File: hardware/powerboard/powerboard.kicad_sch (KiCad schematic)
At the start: 31 parts, among them J1 USB_B_Micro, U1 AP2138N-2.5, U2 MCP1603, U3 RP2040

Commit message: Slight schematic changes
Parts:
- added C19, C20, C21: 1n, Capacitor_SMD:C_0603_1608Metric, symbol Device:C
- added C22: 10u, Capacitor_SMD:C_0603_1608Metric, symbol Device:C
- added R10, R11, R6, R7, R8, R9: 1k, Resistor_SMD:R_0603_1608Metric, symbol Device:R
- added SW1: Oct_Up, Button_Switch_THT:SW_PUSH_6mm, symbol Switch:SW_Push
- added SW2: RESET, Button_Switch_THT:SW_PUSH_6mm, symbol Switch:SW_Push
- added SW3: Oct_Down, Button_Switch_THT:SW_PUSH_6mm, symbol Switch:SW_Push
- C1, C10, C11, C12, C13, C14, C15, C2, C3, C4, C5, C6, C8: footprint (none) -> Capacitor_SMD:C_0603_1608Metric
- C16, C17, C18: renamed from C?; footprint (none) -> Capacitor_SMD:C_0603_1608Metric
- C7, C9: footprint (none) -> Capacitor_SMD:C_0402_1005Metric
- gave numbers to parts that had none: 6
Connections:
- net +3.3V: now also C22.1, R10.1, R6.1, R7.1
- net GND: now also C10.2, C11.2, C12.2, C13.2, C14.2, C15.2, C8.2, C19.2, C20.2, C21.2, C22.2, SW1.1, SW2.1, SW3.1
- net QSPI_SS: now also U3.56 (QSPI_SS)
- net Oct_Up: now reaches U3.31 (GPIO20)
- net Oct_Up: now also C19.1, R8.2
- net Oct_Down: now reaches U3.32 (GPIO21)
- net Oct_Down: now also C21.1, R11.2
- net RESET: now reaches U3.34 (GPIO22)
- net RESET: now also C20.1, R9.2
- new net: R10.2, R11.1, SW3.2
- new net: R6.2, R8.1, SW1.2
- new net: R7.2, R9.1, SW2.2
- no-connect marks 1 -> 5
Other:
- note added: "ADC Reference"
- note added: "Buttons"
- note added: "close to pin 44 0402 foot"
- note added: "close to pin 45 0402 foot"
- note removed: "close to pin 44"
- note removed: "close to pin 45"

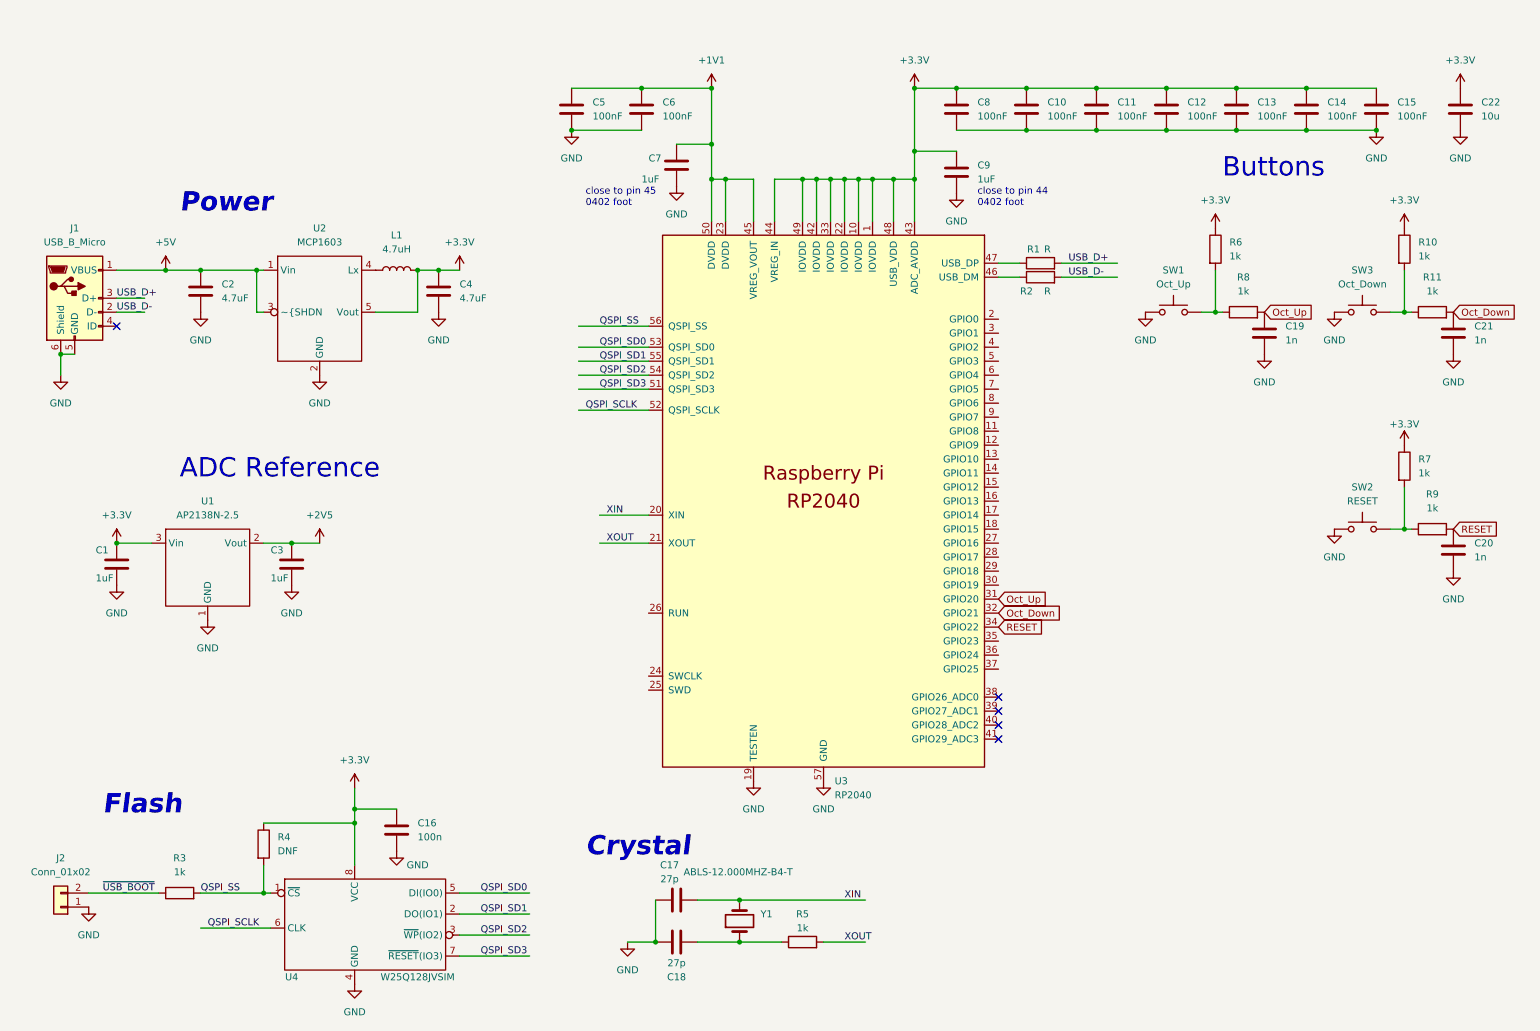
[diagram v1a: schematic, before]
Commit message: Schematic Headers Added, Footprints Updated
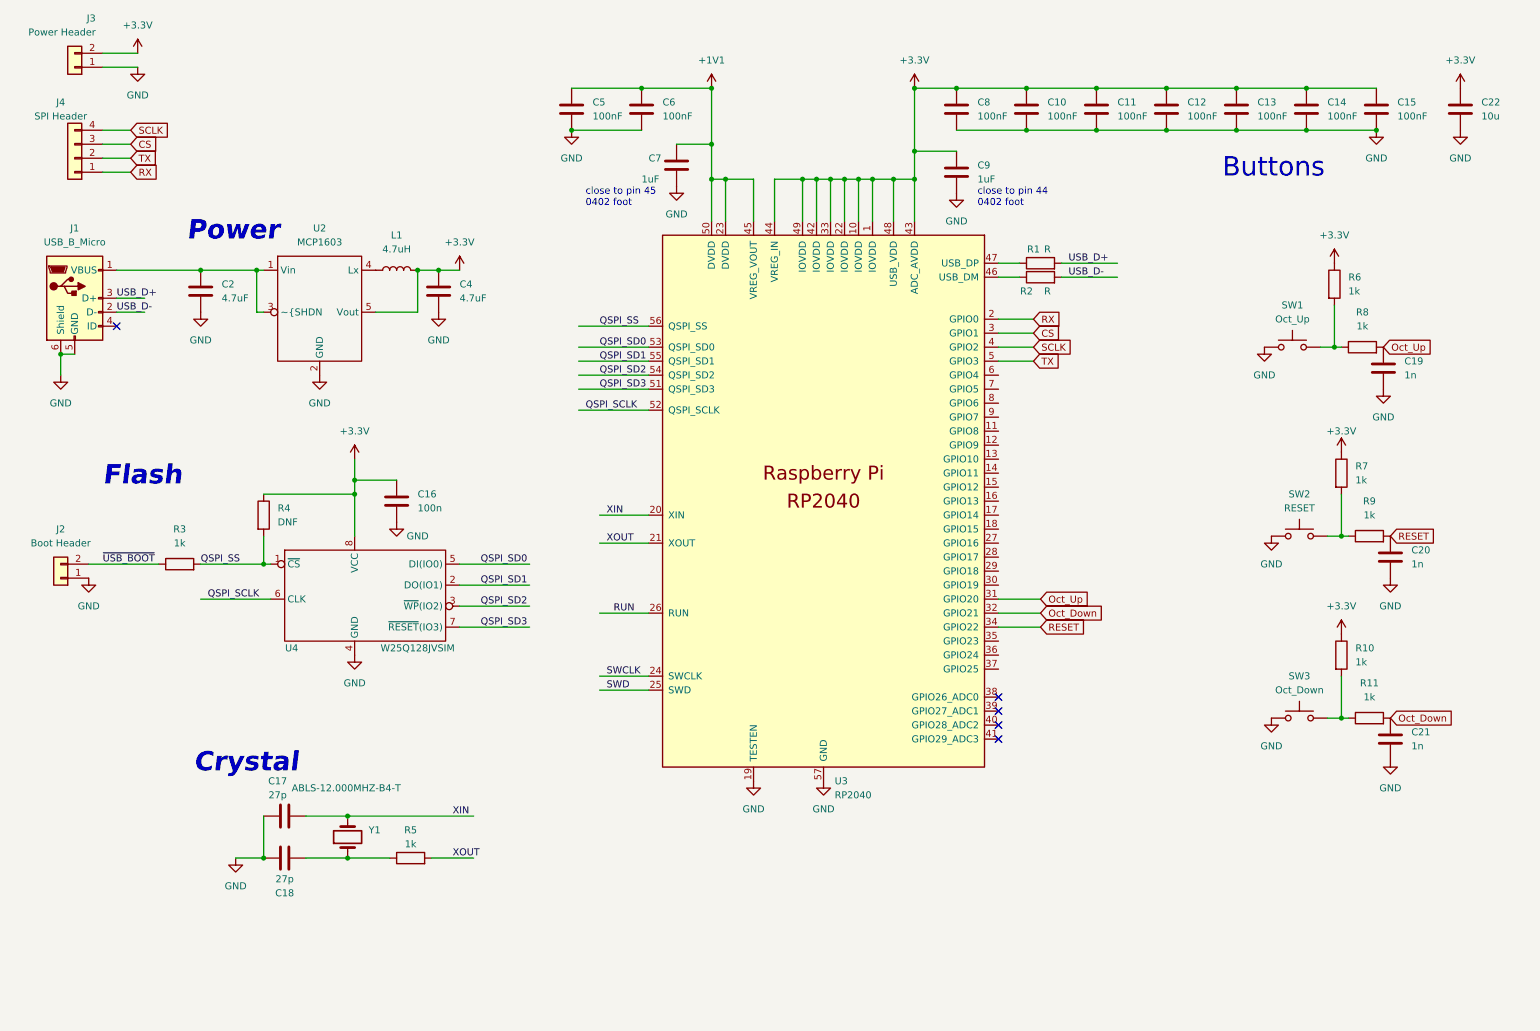
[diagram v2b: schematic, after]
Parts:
- removed C1, C3: 1uF, Capacitor_SMD:C_0603_1608Metric, symbol Device:C
- removed U1: AP2138N-2.5, Package_TO_SOT_SMD:TSOT-23, symbol ece_capstone:AP2138N-2.5
- added J3: Power Header, Connector_PinHeader_2.54mm:PinHeader_1x02_P2.54mm_Vertical, symbol Connector_Generic:Conn_01x02
- added J4: SPI Header, Connector_PinHeader_2.54mm:PinHeader_1x04_P2.54mm_Vertical, symbol Connector_Generic:Conn_01x04
- J1: footprint (none) -> Connector_USB:USB_Micro-B_Molex_47346-0001
- J2: value Conn_01x02 -> Boot Header; footprint (none) -> Connector_PinHeader_2.54mm:PinHeader_1x02_P2.54mm_Vertical
- R1, R2, R3, R4, R5: footprint (none) -> Resistor_SMD:R_0603_1608Metric
- Y1: footprint (none) -> Crystal:Crystal_HC49-4H_Vertical
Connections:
- net +3.3V: now also J3.2 (Pin_2)
- net GND: now also J3.1 (Pin_1)
- net RX: now reaches U3.2 (GPIO0)
- net RX: now also J4.1 (Pin_1)
- net SWCLK: now reaches U3.24 (SWCLK)
- net SWD: now reaches U3.25 (SWD)
- net RUN: now reaches U3.26 (RUN)
- net CS: now reaches U3.3 (GPIO1)
- net CS: now also J4.3 (Pin_3)
- net SCLK: now reaches U3.4 (GPIO2)
- net SCLK: now also J4.4 (Pin_4)
- net TX: now reaches U3.5 (GPIO3)
- net TX: now also J4.2 (Pin_2)
- net +5V: no longer names the net of C2.1, J1.1 (VBUS), U2.1 (Vin), U2.3 (~{SHDN)
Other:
- note removed: "ADC Reference"
- moved on the sheet: C16, C17, C18, C19, C20, C21, J2, R10, R11, R3, R4, R5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

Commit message: Schematics updated, Layout started for powerboard
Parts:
- L1: footprint (none) -> Inductor_SMD:L_1812_4532Metric
- Y1: footprint Crystal:Crystal_HC49-4H_Vertical -> RP2040_minimal:Crystal_SMD_HC49-US
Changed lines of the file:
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@@
     (property "Reference" "L1" (id 0) (at 81.28 55.88 90))
     (property "Value" "4.7uH" (id 1) (at 81.28 58.42 90))
-    (property "Footprint" "" (id 2) (at 81.28 62.23 0)
+    (property "Footprint" "Inductor_SMD:L_1812_4532Metric" (id 2) (at 81.28 62.23 0)
       (effects (font (size 1.27 1.27)) hide)
     )
@@
       (effects (font (size 1.27 1.27)) (justify right))
     )
-    (property "Footprint" "Crystal:Crystal_HC49-4H_Vertical" (id 2) (at 72.39 165.1 0)
+    (property "Footprint" "RP2040_minimal:Crystal_SMD_HC49-US" (id 2) (at 72.39 165.1 0)
       (effects (font (size 1.27 1.27)) hide)
     )
@@
     )
     (path "/985ac95d-4079-4633-83a9-2b6fdcd0332b"
-      (reference "L1") (unit 1) (value "4.7uH") (footprint "")
+      (reference "L1") (unit 1) (value "4.7uH") (footprint "Inductor_SMD:L_1812_4532Metric")
     )
     (path "/2035ea6c-6ade-4ffb-9114-438bd049019e"
@@
     )
     (path "/e2e2bf3f-d1e0-4862-acaf-b79cbebcb3a1"
-      (reference "Y1") (unit 1) (value "ABLS-12.000MHZ-B4-T") (footprint "Crystal:Crystal_HC49-4H_Vertical")
-    )
-  )
+      (reference "Y1") (unit 1) (value "ABLS-12.000MHZ-B4-T") (footprint "RP2040_minimal:Crystal_SMD_HC49-US")
+    )
+  )

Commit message: Powerboard PCB Started
Powerboard PCB Started
Placed and Routed Power Section, USB Port, Power Header, All Bypass Capacitors, USB Data Lines.
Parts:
- C10, C11, C12, C13, C14, C15, C5, C6, C8: footprint Capacitor_SMD:C_0603_1608Metric -> Capacitor_SMD:C_0402_1005Metric
- R1, R2: value R -> 27; footprint Resistor_SMD:R_0603_1608Metric -> Resistor_SMD:R_0402_1005Metric
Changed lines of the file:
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@@
     (in_bom yes) (on_board yes)
     (property "Reference" "R1" (id 0) (at 196.85 58.42 90))
-    (property "Value" "R" (id 1) (at 199.39 58.42 90))
-    (property "Footprint" "Resistor_SMD:R_0603_1608Metric" (id 2) (at 198.12 62.738 90)
+    (property "Value" "27" (id 1) (at 199.39 58.42 90))
+    (property "Footprint" "Resistor_SMD:R_0402_1005Metric" (id 2) (at 198.12 62.738 90)
       (effects (font (size 1.27 1.27)) hide)
     )
@@
       (effects (font (size 1.27 1.27)) (justify left))
     )
-    (property "Footprint" "Capacitor_SMD:C_0603_1608Metric" (id 2) (at 183.8452 36.83 0)
+    (property "Footprint" "Capacitor_SMD:C_0402_1005Metric" (id 2) (at 183.8452 36.83 0)
       (effects (font (size 1.27 1.27)) hide)
     )
@@
       (effects (font (size 1.27 1.27)) (justify left))
     )
-    (property "Footprint" "Capacitor_SMD:C_0603_1608Metric" (id 2) (at 247.3452 36.83 0)
+    (property "Footprint" "Capacitor_SMD:C_0402_1005Metric" (id 2) (at 247.3452 36.83 0)
       (effects (font (size 1.27 1.27)) hide)
     )
@@
       (effects (font (size 1.27 1.27)) (justify left))
     )
-    (property "Footprint" "Capacitor_SMD:C_0603_1608Metric" (id 2) (at 209.2452 36.83 0)
+    (property "Footprint" "Capacitor_SMD:C_0402_1005Metric" (id 2) (at 209.2452 36.83 0)
       (effects (font (size 1.27 1.27)) hide)
     )
@@
       (effects (font (size 1.27 1.27)) (justify left))
     )
-    (property "Footprint" "Capacitor_SMD:C_0603_1608Metric" (id 2) (at 196.5452 36.83 0)
+    (property "Footprint" "Capacitor_SMD:C_0402_1005Metric" (id 2) (at 196.5452 36.83 0)
       (effects (font (size 1.27 1.27)) hide)
     )
@@
       (effects (font (size 1.27 1.27)) (justify left))
     )
-    (property "Footprint" "Capacitor_SMD:C_0603_1608Metric" (id 2) (at 126.6952 36.83 0)
+    (property "Footprint" "Capacitor_SMD:C_0402_1005Metric" (id 2) (at 126.6952 36.83 0)
       (effects (font (size 1.27 1.27)) hide)
     )
@@
       (effects (font (size 1.27 1.27)) (justify left))
     )
-    (property "Footprint" "Capacitor_SMD:C_0603_1608Metric" (id 2) (at 113.9952 36.83 0)
+    (property "Footprint" "Capacitor_SMD:C_0402_1005Metric" (id 2) (at 113.9952 36.83 0)
       (effects (font (size 1.27 1.27)) hide)
     )
@@
     (in_bom yes) (on_board yes)
     (property "Reference" "R2" (id 0) (at 195.58 66.04 90))
-    (property "Value" "R" (id 1) (at 199.39 66.04 90))
-    (property "Footprint" "Resistor_SMD:R_0603_1608Metric" (id 2) (at 198.12 65.278 90)
+    (property "Value" "27" (id 1) (at 199.39 66.04 90))
+    (property "Footprint" "Resistor_SMD:R_0402_1005Metric" (id 2) (at 198.12 65.278 90)
       (effects (font (size 1.27 1.27)) hide)
     )
@@
       (effects (font (size 1.27 1.27)) (justify left))
     )
-    (property "Footprint" "Capacitor_SMD:C_0603_1608Metric" (id 2) (at 221.9452 36.83 0)
+    (property "Footprint" "Capacitor_SMD:C_0402_1005Metric" (id 2) (at 221.9452 36.83 0)
       (effects (font (size 1.27 1.27)) hide)
     )
@@
       (effects (font (size 1.27 1.27)) (justify left))
     )
-    (property "Footprint" "Capacitor_SMD:C_0603_1608Metric" (id 2) (at 234.6452 36.83 0)
+    (property "Footprint" "Capacitor_SMD:C_0402_1005Metric" (id 2) (at 234.6452 36.83 0)
       (effects (font (size 1.27 1.27)) hide)
     )
@@
       (effects (font (size 1.27 1.27)) (justify left))
     )
-    (property "Footprint" "Capacitor_SMD:C_0603_1608Metric" (id 2) (at 260.0452 36.83 0)
+    (property "Footprint" "Capacitor_SMD:C_0402_1005Metric" (id 2) (at 260.0452 36.83 0)
       (effects (font (size 1.27 1.27)) hide)
     )
@@
     )
     (path "/62a559f3-0287-407e-b429-1597a5ab7b86"
-      (reference "C5") (unit 1) (value "100nF") (footprint "Capacitor_SMD:C_0603_1608Metric")
+      (reference "C5") (unit 1) (value "100nF") (footprint "Capacitor_SMD:C_0402_1005Metric")
     )
     (path "/443b80eb-d007-4ce3-9f3b-469888004f5e"
-      (reference "C6") (unit 1) (value "100nF") (footprint "Capacitor_SMD:C_0603_1608Metric")
+      (reference "C6") (unit 1) (value "100nF") (footprint "Capacitor_SMD:C_0402_1005Metric")
     )
     (path "/5b88a535-7c41-4e18-839c-83119a636fc4"
@@
     )
     (path "/28843f88-5955-46ce-b048-ceb8dce5610b"
-      (reference "C8") (unit 1) (value "100nF") (footprint "Capacitor_SMD:C_0603_1608Metric")
+      (reference "C8") (unit 1) (value "100nF") (footprint "Capacitor_SMD:C_0402_1005Metric")
     )
     (path "/9684e144-002c-4761-8aee-b34da0ec76fa"
@@
     )
     (path "/3d773b17-92e2-4074-af14-a6e489f1893d"
-      (reference "C10") (unit 1) (value "100nF") (footprint "Capacitor_SMD:C_0603_1608Metric")
+      (reference "C10") (unit 1) (value "100nF") (footprint "Capacitor_SMD:C_0402_1005Metric")
     )
     (path "/3d49a749-be03-431d-bbc9-f17f0c5abb00"
-      (reference "C11") (unit 1) (value "100nF") (footprint "Capacitor_SMD:C_0603_1608Metric")
+      (reference "C11") (unit 1) (value "100nF") (footprint "Capacitor_SMD:C_0402_1005Metric")
     )
     (path "/9b96e68f-9279-41a7-9805-7c6c1ae5daba"
-      (reference "C12") (unit 1) (value "100nF") (footprint "Capacitor_SMD:C_0603_1608Metric")
+      (reference "C12") (unit 1) (value "100nF") (footprint "Capacitor_SMD:C_0402_1005Metric")
     )
     (path "/d7b1d657-77eb-4fba-bbd5-eebd98750d26"
-      (reference "C13") (unit 1) (value "100nF") (footprint "Capacitor_SMD:C_0603_1608Metric")
+      (reference "C13") (unit 1) (value "100nF") (footprint "Capacitor_SMD:C_0402_1005Metric")
     )
     (path "/3a25c00b-d034-4560-8d23-f650e7a6bfd4"
-      (reference "C14") (unit 1) (value "100nF") (footprint "Capacitor_SMD:C_0603_1608Metric")
+      (reference "C14") (unit 1) (value "100nF") (footprint "Capacitor_SMD:C_0402_1005Metric")
     )
     (path "/f391a5ac-d2ed-4eee-80c9-3a876f03353f"
-      (reference "C15") (unit 1) (value "100nF") (footprint "Capacitor_SMD:C_0603_1608Metric")
+      (reference "C15") (unit 1) (value "100nF") (footprint "Capacitor_SMD:C_0402_1005Metric")
     )
     (path "/d94ce941-d973-4d50-9dcc-a718392ddb9d"
@@
     )
     (path "/2035ea6c-6ade-4ffb-9114-438bd049019e"
-      (reference "R1") (unit 1) (value "R") (footprint "Resistor_SMD:R_0603_1608Metric")
+      (reference "R1") (unit 1) (value "27") (footprint "Resistor_SMD:R_0402_1005Metric")
     )
     (path "/6cc77f12-c67f-440c-852a-be4a938376b5"
-      (reference "R2") (unit 1) (value "R") (footprint "Resistor_SMD:R_0603_1608Metric")
+      (reference "R2") (unit 1) (value "27") (footprint "Resistor_SMD:R_0402_1005Metric")
     )
     (path "/9ae6d505-4ef6-40ba-af4b-5835ede54a03"
